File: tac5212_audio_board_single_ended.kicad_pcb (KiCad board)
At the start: 4 copper layers, 42 x 26.5 mm, 94 parts, among them J1002 TAC5212, U1 Single Buffer - 74LVC1G125GV,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, U2 3.3v LDO - TLV74133PDBVR

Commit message: UPDATE
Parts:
- added G108: jumper, project_fp:jumper_slice, B.Cu at (122.1, 115.1)
- moved C17 0.50 mm to (103.6, 111.4)
- moved C15 0.46 mm to (105.6, 109.2)
- moved C13 0.42 mm to (102.4, 109.9)
- moved OM2 0.30 mm to (104.2, 106.7)
- turned E1 to 90 degrees
- turned E2 to 90 degrees
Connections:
- E1 pad 1: Net-(E1-A) -> Earth
- E1 pad 2: Earth -> Net-(E1-B)
- E2 pad 1: Net-(E2-A) -> Earth
- E2 pad 2: Earth -> Net-(E2-B)
- T*C1 pad 2: GNDD -> Net-(G108-A)
- T*C2 pad 2: GNDD -> Net-(G108-A)
- T*C3 pad 2: GNDD -> Net-(G108-A)
- U2 pad 2: GNDD -> Net-(G108-A)
- board_outline1 pad 49: Net-(E1-A) -> Net-(E1-B)
- board_outline1 pad 50: Net-(E2-A) -> Net-(E2-B)
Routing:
- net (no net): track 28.9 -> 0.00 mm
- net GNDD: track 42.7 -> 21.9 mm
- net Net-(G108-A): track 0.00 -> 15.5 mm
- net Earth: track 157.7 -> 167.5 mm, vias 1 -> 2
- net Net-(E2-B): track 0.00 -> 3.02 mm
- net Net-(E1-B): track 0.00 -> 2.97 mm
- net Net-(U1-Y): track 0.00 -> 1.90 mm
- net 3.3V_LDO: track 90.1 -> 91.4 mm
- net Net-(J1002-VREF): track 3.46 -> 2.85 mm
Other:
- outline, holes or cut-outs redrawn

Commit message: update
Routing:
- net Earth: track 167.5 -> 195.1 mm
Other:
- board text removed: "HP (TOP) IN2 (BOT)"
- board text removed: "HP2 OUT"
- board text removed: "IN1"

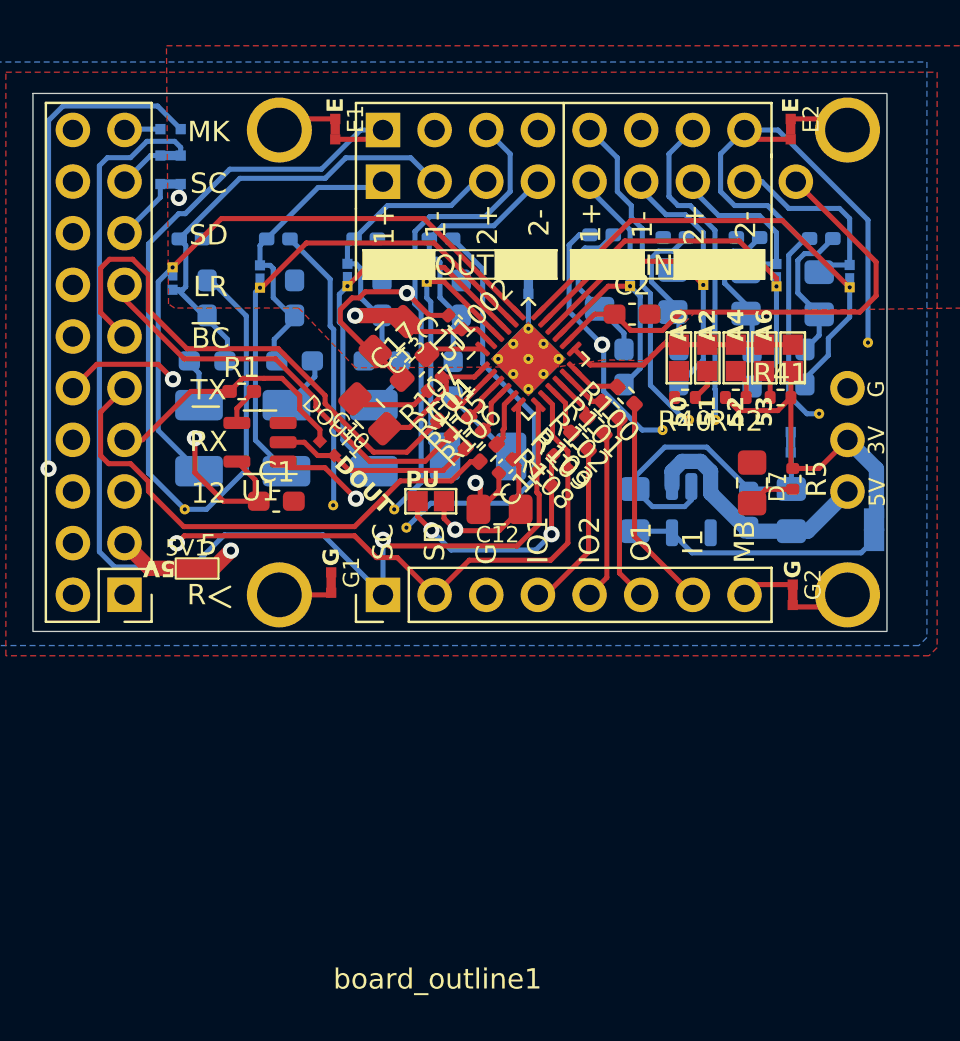
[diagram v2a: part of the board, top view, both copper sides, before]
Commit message: added enable (held-high)
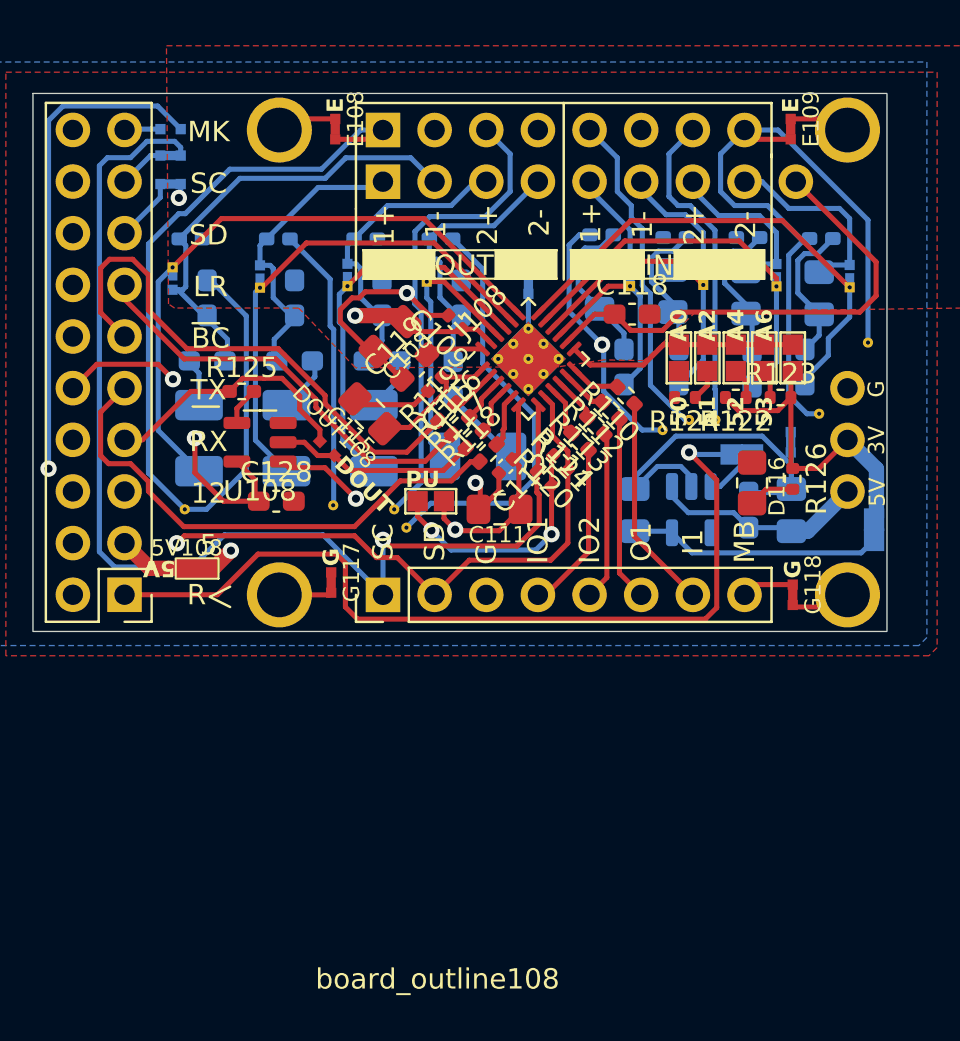
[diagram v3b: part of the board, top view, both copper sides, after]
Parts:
- added ENABLE108: jumper, project_fp:jumper_slice_1mm, B.Cu at (119.7, 115.7)
- renumbered 3V3 to 3V108, 5V1 to 5V108, ADD1001 to ADD108, ADD1 to ADD109, ADD1003 to ADD110, ADD1004 to ADD111, ADD1002 to ADD112, C13 to C108, C15 to C109, C18 to C110, C12 to C111, C14 to C112, C22 to C113, C19 to C114, C10 to C115, C11 to C116, C23 to C117, C2 to C118, C17 to C119, C20 to C120, C24 to C121, C21 to C122, C25 to C123, C1012 to C124, C1009 to C125, C1010 to C126, C1011 to C127, C1 to C128, D17 to D108, D18 to D109, D19 to D110, D20 to D111, D1005 to D112, D1002 to D113, D1003 to D114, D1004 to D115, D7 to D116, DOUT1 to DOUT108, E1 to E108, E2 to E109, FB1001 to FB108, FB1002 to FB109, FB1003 to FB110, FB1004 to FB111, G11 to G108, G5 to G109, G4 to G110, G3 to G111, G6 to G112, G7 to G113, G8 to G114, G9 to G115, G10 to G116, G1 to G117, G2 to G118, G108 to G119, GND1 to GND108, INM2 to INM108, INM1 to INM109, INP2 to INP108, INP1 to INP109, J1002 to J108, MCLK1 to MCLK108, OM1 to OM108, OM2 to OM109, OP1 to OP108, OP2 to OP109, PU_EN1001 to PU_EN108, R17 to R108, R18 to R109, R100 to R110, R19 to R111, R101 to R112, R102 to R113, R103 to R114, R104 to R115, R20 to R116, R105 to R117, R106 to R118, R107 to R119, R108 to R120, R109 to R121, R42 to R122, R41 to R123, R40 to R124, R1 to R125, R5 to R126, SCL1001 to SCL108, SDA1001 to SDA108, T*C1 to T*C108, T*C2 to T*C109, T*C3 to T*C110, U1 to U108, U2 to U109, board_outline1 to board_outline108
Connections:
- U109 pad 3: 5V -> Net-(ENABLE108-B)
- board_outline108 pad 1: unconnected-(board_outline1-HELD_HIGH-Pad1) -> EN_HELD_HIGH
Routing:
- net EN_HELD_HIGH: track 0.00 -> 43.1 mm, vias 0 -> 1
- net Net-(G119-A): track 15.5 -> 18.8 mm
- net Net-(ENABLE108-B): track 0.00 -> 2.69 mm
- net 5V: track 46.0 -> 44.2 mm

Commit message: update
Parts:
- removed ENABLE108: jumper, project_fp:jumper_slice_1mm
- added C129: 1uF, Capacitor_SMD:C_0603_1608Metric_Pad1.08x0.95mm_HandSolder, B.Cu at (112.5, 116.8)
- added R127: 0 Ohm, Resistor_SMD:R_0402_1005Metric_Pad0.72x0.64mm_HandSolder, B.Cu at (119.4, 115.7)
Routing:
- net EN_HELD_HIGH: track 43.1 -> 55.6 mm
- net Net-(G119-A): track 18.8 -> 11.9 mm
- net GNDD: track 21.9 -> 28.7 mm, vias 3 -> 4
- net 5V: track 44.2 -> 46.1 mm
- net 5212_SCL: track 57.0 -> 58.6 mm
- net 3.3V_LDO: track 91.4 -> 92.9 mm
- net 3.3V_A: track 12.5 -> 13.2 mm

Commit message: update
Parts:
- moved G109 1.08 mm to (99.2, 117.2)
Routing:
- net GNDD: track 28.7 -> 38.5 mm, vias 4 -> 6
- net EN_HELD_HIGH: track 55.6 -> 47.7 mm
- net 5212_SCL: track 58.6 -> 59.9 mm
- net Earth: track 195.1 -> 194.3 mm

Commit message: update
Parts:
- removed ADD109: jumper, project_fp:SolderJumper-2_Open_Pad0.5x1.0mm_ADDR
- TAC5212: renamed from J108; footprint project_fp:TAC5212IRGER-24-1EP_4x4mm -> project_fp:VQFN-24-1EP_4x4mm_P0.5mm_EP2.45x2.45mm_ThermalVias
- moved ADD111 1.00 mm to (121.8, 111.0)
- moved GND108 0.90 mm to (109.2, 106.4)
- moved ADD110 0.80 mm to (120.2, 111.0)
- moved ADD112 0.60 mm to (118.6, 111.0)
- moved ADD108 0.40 mm to (117.0, 111.0)
- moved C108 0.40 mm to (102.0, 109.9)
- moved C119 0.40 mm to (103.2, 111.4)
- moved C112 0.33 mm to (108.2, 116.6), turned to 45 degrees
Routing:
- net GNDD: track 38.5 -> 49.2 mm
- net 3.3V_LDO: track 92.9 -> 83.9 mm
- net Net-(TAC5212-ADDR): track 11.5 -> 10.8 mm

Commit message: update
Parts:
- moved C112 0.28 mm to (108.4, 116.4)
- renumbered INM109 to INM1, INM108 to INM2, INP109 to INP1, INP108 to INP2, OM108 to OM1, OM109 to OM2, OP108 to OP1, OP109 to OP2
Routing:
- net GNDD: track 49.2 -> 57.6 mm, vias 6 -> 15
- net 3.3V_LDO: track 83.9 -> 86.5 mm
- net Earth: track 194.0 -> 194.7 mm, vias 2 -> 10
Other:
- board text removed: "TAC5212 AUDIO BOARD SE © 2023 JAY SHOEMAKER"
